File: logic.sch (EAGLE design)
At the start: 8 parts, among them CON1 PINHEAD_1X10-2, CON2 PINHEAD_1X10-2, CON3 PINHEAD_1X02-2, CON4 PINHEAD_1X02-2, CON5 PINHEAD_1X02-2, CON6 PINHEAD_1X02-2, CON7 PINHEAD_1X07-2

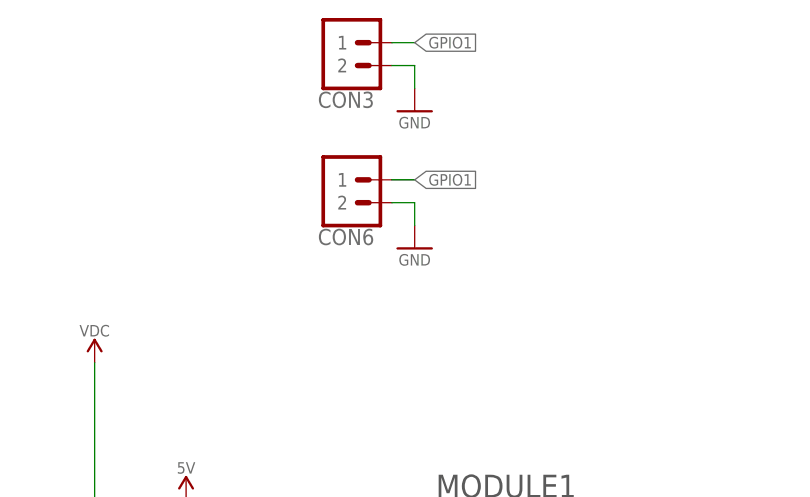
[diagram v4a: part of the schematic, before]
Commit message: fixed logic board to fit housing  better
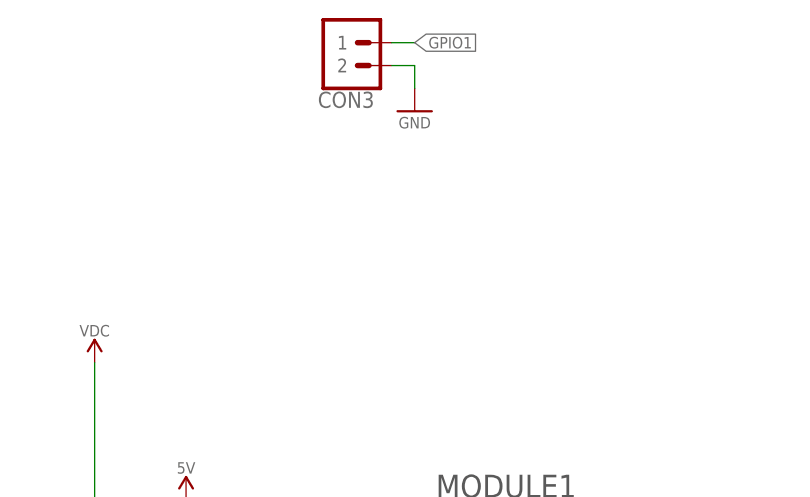
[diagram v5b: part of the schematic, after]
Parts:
- removed CON6: PINHEAD_1X02-2, pinhead:PINHEAD_1X02-2
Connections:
- net GND: no longer CON6.2
- net GPIO1: no longer CON6.1
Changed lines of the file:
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@@
 <part name="CON1" library="pinhead" library_urn="urn:adsk.eagle:library:2540341" deviceset="PINHEAD_1X10" device="-2" package3d_urn="urn:adsk.eagle:package:6503373/2"/>
 <part name="CON2" library="pinhead" library_urn="urn:adsk.eagle:library:2540341" deviceset="PINHEAD_1X10" device="-2" package3d_urn="urn:adsk.eagle:package:6503373/2"/>
-<part name="MODULE1" library="zubax_modules" library_urn="urn:adsk.eagle:library:5014895" deviceset="MITOHONDRIQUE" device="-TH" package3d_urn="urn:adsk.eagle:package:4410646/10"/>
+<part name="MODULE1" library="zubax_modules" library_urn="urn:adsk.eagle:library:5014895" deviceset="MITOHONDRIQUE" device="-TH" package3d_urn="urn:adsk.eagle:package:4410646/11"/>
 <part name="+P1" library="supply_symbols" library_urn="urn:adsk.eagle:library:5017758" deviceset="5V" device=""/>
-<part name="CON4" library="pinhead" library_urn="urn:adsk.eagle:library:2540341" deviceset="PINHEAD_1X02" device="-2" package3d_urn="urn:adsk.eagle:package:6503394/3"/>
-<part name="CON5" library="pinhead" library_urn="urn:adsk.eagle:library:2540341" deviceset="PINHEAD_1X02" device="-2" package3d_urn="urn:adsk.eagle:package:6503394/3"/>
-<part name="CON6" library="pinhead" library_urn="urn:adsk.eagle:library:2540341" deviceset="PINHEAD_1X02" device="-2" package3d_urn="urn:adsk.eagle:package:6503394/3">
-<variant name="BASIC" populate="no"/>
-</part>
-<part name="GND2" library="supply_symbols" library_urn="urn:adsk.eagle:library:5017758" deviceset="GND" device="" value="GND"/>
+<part name="CON4" library="pinhead" library_urn="urn:adsk.eagle:library:2540341" deviceset="PINHEAD_1X02" device="-2" package3d_urn="urn:adsk.eagle:package:6503394/4"/>
+<part name="CON5" library="pinhead" library_urn="urn:adsk.eagle:library:2540341" deviceset="PINHEAD_1X02" device="-2" package3d_urn="urn:adsk.eagle:package:6503394/4"/>
 <part name="GND3" library="supply_symbols" library_urn="urn:adsk.eagle:library:5017758" deviceset="GND" device="" value="GND"/>
 <part name="+P3" library="supply_symbols" library_urn="urn:adsk.eagle:library:5017758" deviceset="5V" device=""/>
 <part name="CON7" library="pinhead" library_urn="urn:adsk.eagle:library:2540341" deviceset="PINHEAD_1X07" device="-2" package3d_urn="urn:adsk.eagle:package:2540391/3"/>
-<part name="CON3" library="pinhead" library_urn="urn:adsk.eagle:library:2540341" deviceset="PINHEAD_1X02" device="-2" package3d_urn="urn:adsk.eagle:package:6503394/3">
+<part name="CON3" library="pinhead" library_urn="urn:adsk.eagle:library:2540341" deviceset="PINHEAD_1X02" device="-2" package3d_urn="urn:adsk.eagle:package:6503394/4">
 <variant name="BASIC" populate="no"/>
 </part>
@@
 <attribute name="NAME" x="266.7" y="186.69" size="1.778" layer="95" font="vector" ratio="15" rot="R180" align="center"/>
 </instance>
-<instance part="CON6" gate="G$1" x="111.76" y="198.12" smashed="yes" rot="MR180">
-<attribute name="NAME" x="114.3" y="189.23" size="1.778" layer="95" font="vector" ratio="15" rot="MR180" align="center"/>
-</instance>
-<instance part="GND2" gate="1" x="121.92" y="187.96" smashed="yes">
-<attribute name="VALUE" x="121.92" y="186.69" size="1.27" layer="96" font="vector" ratio="15" align="center"/>
-</instance>
 <instance part="GND3" gate="1" x="259.08" y="185.42" smashed="yes" rot="MR0">
 <attribute name="VALUE" x="259.08" y="184.15" size="1.27" layer="96" font="vector" ratio="15" rot="MR0" align="center"/>
@@
 <junction x="93.98" y="154.94"/>
 <label x="50.8" y="154.94" size="1.27" layer="95"/>
-</segment>
-<segment>
-<pinref part="GND2" gate="1" pin="GND"/>
-<wire x1="121.92" y1="193.04" x2="121.92" y2="190.5" width="0.1524" layer="91"/>
-<pinref part="CON6" gate="G$1" pin="2"/>
-<wire x1="121.92" y1="193.04" x2="119.38" y2="193.04" width="0.1524" layer="91"/>
 </segment>
 <segment>
@@
 </segment>
 <segment>
-<pinref part="CON6" gate="G$1" pin="1"/>
-<wire x1="119.38" y1="195.58" x2="121.92" y2="195.58" width="0.1524" layer="91"/>
-<label x="121.92" y="195.58" size="1.27" layer="95" xref="yes"/>
-</segment>
-<segment>

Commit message: let there be a giant hole in the middle of the PCB
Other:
- note added: "Connector PCB connection"
- note added: "Thermistor connection"
- moved on the sheet: CON1, CON2, CON3, CON4, CON5, CON7, MODULE1

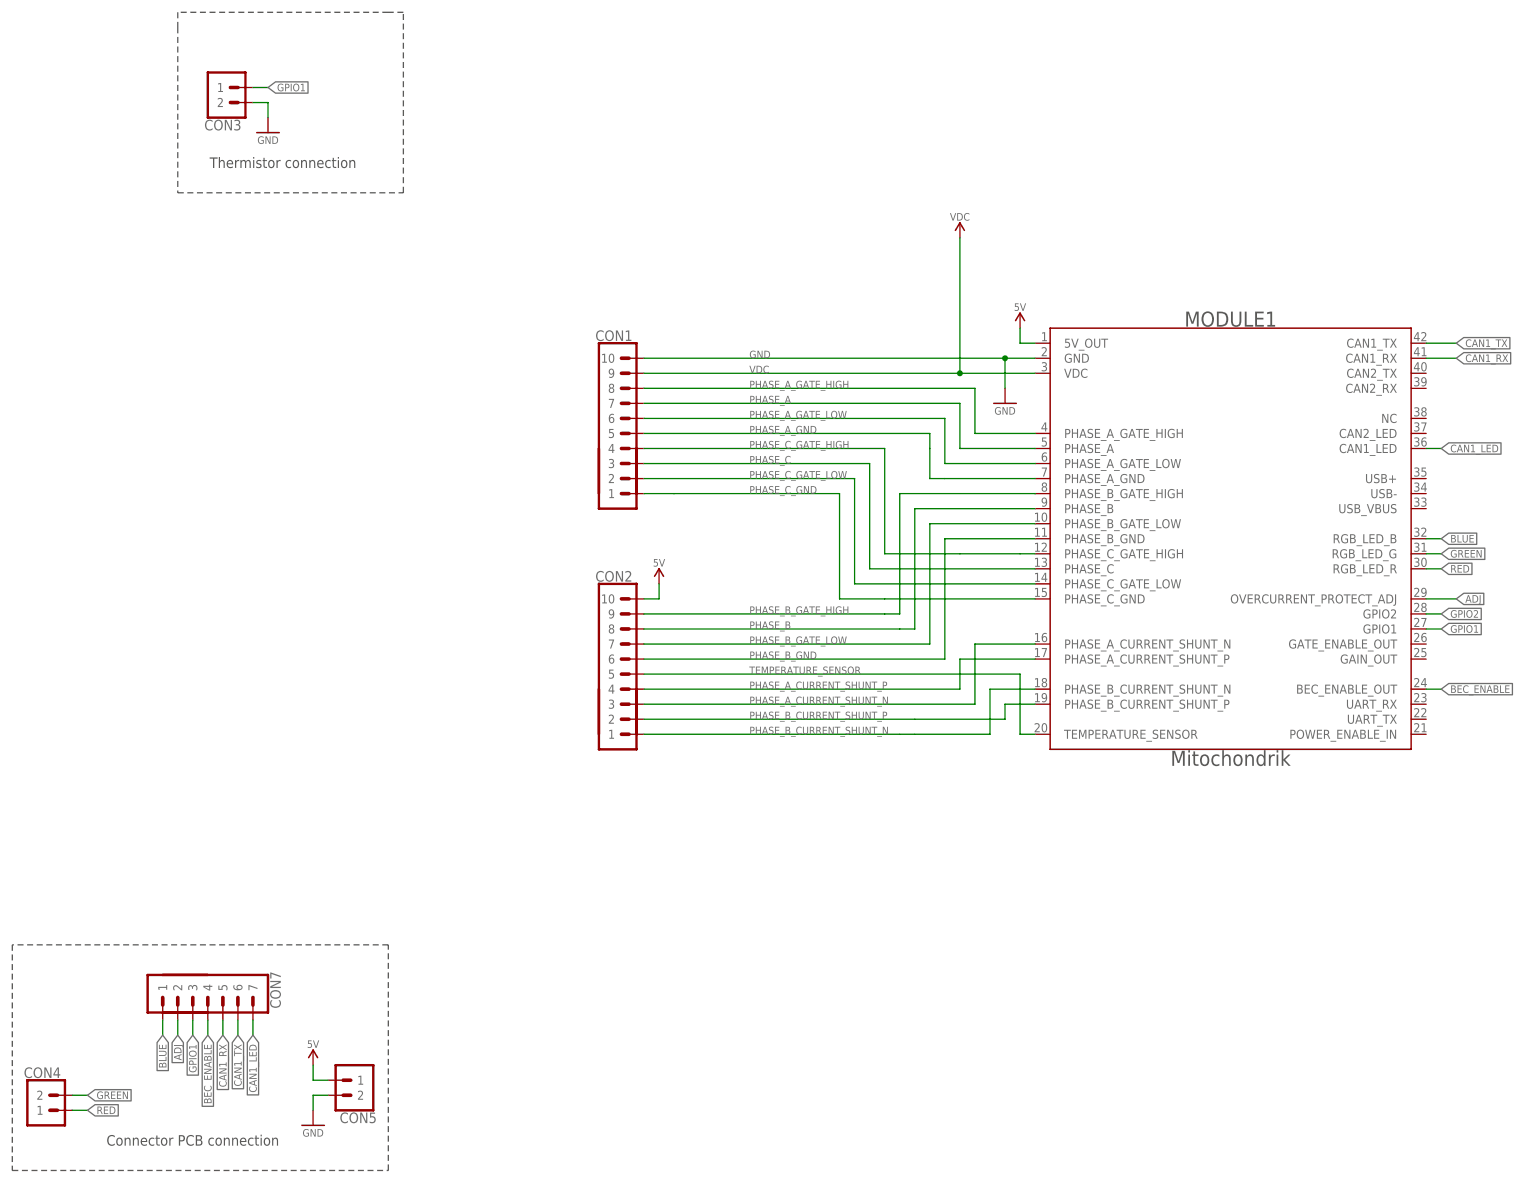
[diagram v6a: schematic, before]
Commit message: migration to the latest version of mitochondrik library
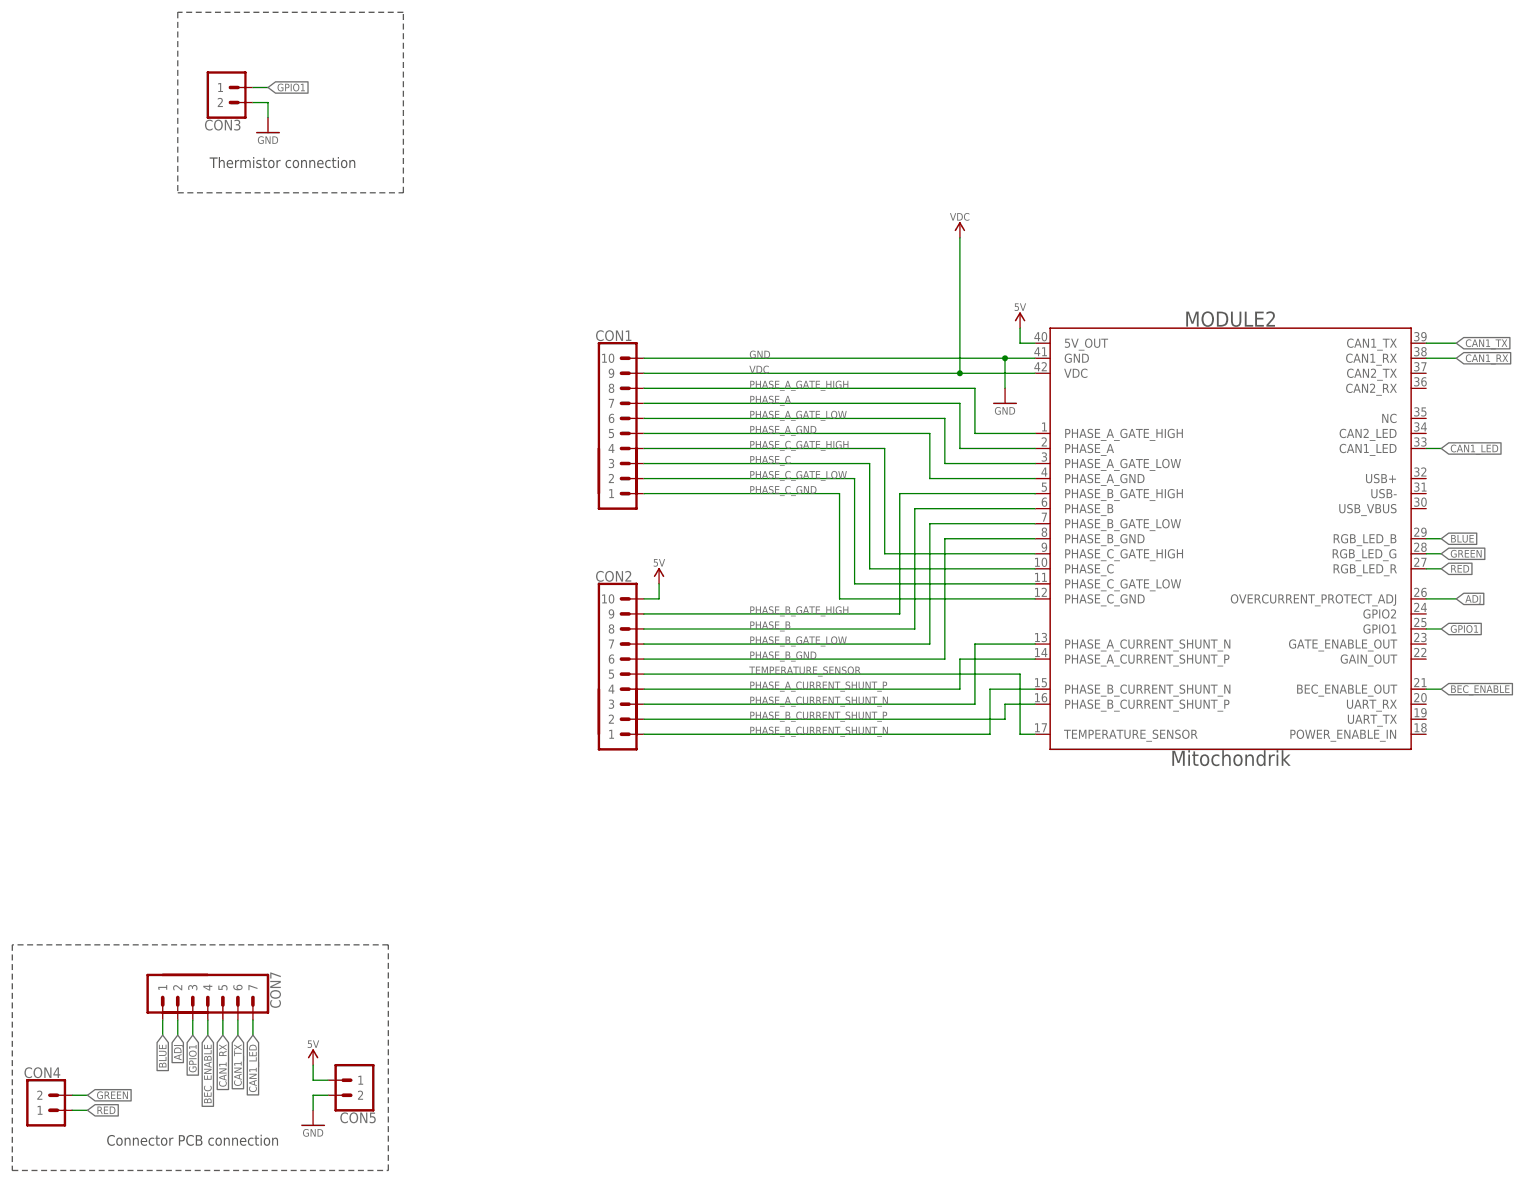
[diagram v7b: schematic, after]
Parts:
- removed MODULE1: MITOHONDRIQUE-TH, zubax_modules:MITOHONDRIQUE-TH
- added MODULE2: MITOHONDRIQUE_V0.2-TH, zubax_modules:MITOHONDRIQUE_V0.2-TH
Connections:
- removed net GPIO2: MODULE1.GPIO2
- net ADJ: now also MODULE2.OVERCURRENT_PROTECT_ADJ; no longer MODULE1.OVERCURRENT_PROTECT_ADJ
- net BEC_ENABLE: now also MODULE2.BEC_ENABLE_OUT; no longer MODULE1.BEC_ENABLE_OUT
- net BLUE: now also MODULE2.RGB_LED_B; no longer MODULE1.RGB_LED_B
- net CAN1_LED: now also MODULE2.CAN1_LED; no longer MODULE1.CAN1_LED
- net CAN1_RX: now also MODULE2.CAN1_RX; no longer MODULE1.CAN1_RX
- net CAN1_TX: now also MODULE2.CAN1_TX; no longer MODULE1.CAN1_TX
- net GND: now also MODULE2.GND; no longer MODULE1.GND
- net GPIO1: now also MODULE2.GPIO1; no longer MODULE1.GPIO1
- net GREEN: now also MODULE2.RGB_LED_G; no longer MODULE1.RGB_LED_G
- net PHASE_A: now also MODULE2.PHASE_A; no longer MODULE1.PHASE_A
- net PHASE_A_CURRENT_SHUNT_N: now also MODULE2.PHASE_A_CURRENT_SHUNT_N; no longer MODULE1.PHASE_A_CURRENT_SHUNT_N
- net PHASE_A_CURRENT_SHUNT_P: now also MODULE2.PHASE_A_CURRENT_SHUNT_P; no longer MODULE1.PHASE_A_CURRENT_SHUNT_P
- net PHASE_A_GATE_HIGH: now also MODULE2.PHASE_A_GATE_HIGH; no longer MODULE1.PHASE_A_GATE_HIGH
- net PHASE_A_GATE_LOW: now also MODULE2.PHASE_A_GATE_LOW; no longer MODULE1.PHASE_A_GATE_LOW
- net PHASE_A_GND: now also MODULE2.PHASE_A_GND; no longer MODULE1.PHASE_A_GND
- net PHASE_B: now also MODULE2.PHASE_B; no longer MODULE1.PHASE_B
- net PHASE_B_CURRENT_SHUNT_N: now also MODULE2.PHASE_B_CURRENT_SHUNT_N; no longer MODULE1.PHASE_B_CURRENT_SHUNT_N
- net PHASE_B_CURRENT_SHUNT_P: now also MODULE2.PHASE_B_CURRENT_SHUNT_P; no longer MODULE1.PHASE_B_CURRENT_SHUNT_P
- net PHASE_B_GATE_HIGH: now also MODULE2.PHASE_B_GATE_HIGH; no longer MODULE1.PHASE_B_GATE_HIGH
- net PHASE_B_GATE_LOW: now also MODULE2.PHASE_B_GATE_LOW; no longer MODULE1.PHASE_B_GATE_LOW
- net PHASE_B_GND: now also MODULE2.PHASE_B_GND; no longer MODULE1.PHASE_B_GND
- net PHASE_C: now also MODULE2.PHASE_C; no longer MODULE1.PHASE_C
- net PHASE_C_GATE_HIGH: now also MODULE2.PHASE_C_GATE_HIGH; no longer MODULE1.PHASE_C_GATE_HIGH
- net PHASE_C_GATE_LOW: now also MODULE2.PHASE_C_GATE_LOW; no longer MODULE1.PHASE_C_GATE_LOW
- net PHASE_C_GND: now also MODULE2.PHASE_C_GND; no longer MODULE1.PHASE_C_GND
- net RED: now also MODULE2.RGB_LED_R; no longer MODULE1.RGB_LED_R
- net TEMPERATURE_SENSOR: now also MODULE2.TEMPERATURE_SENSOR; no longer MODULE1.TEMPERATURE_SENSOR
- net VDC: now also MODULE2.VDC; no longer MODULE1.VDC
- net VDD_5V: now also MODULE2.5V_OUT; no longer MODULE1.5V_OUT
